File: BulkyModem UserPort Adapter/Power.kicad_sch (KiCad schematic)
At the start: 14 parts, among them Q1 2N3904, Q2 2N3904

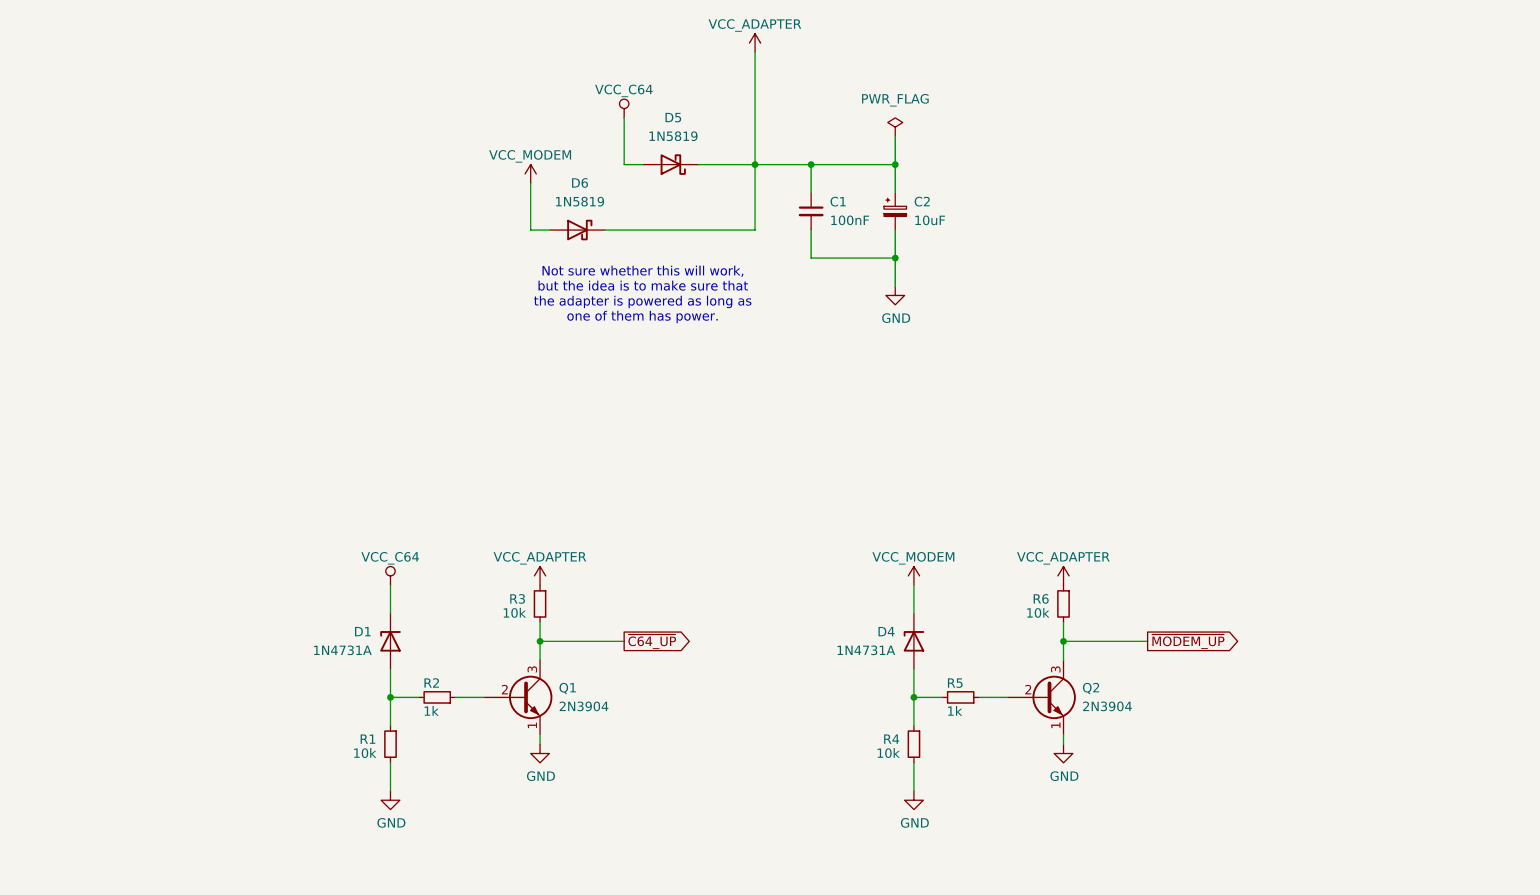
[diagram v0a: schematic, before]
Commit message: Change UserPort transmitter to only enable on both parties present
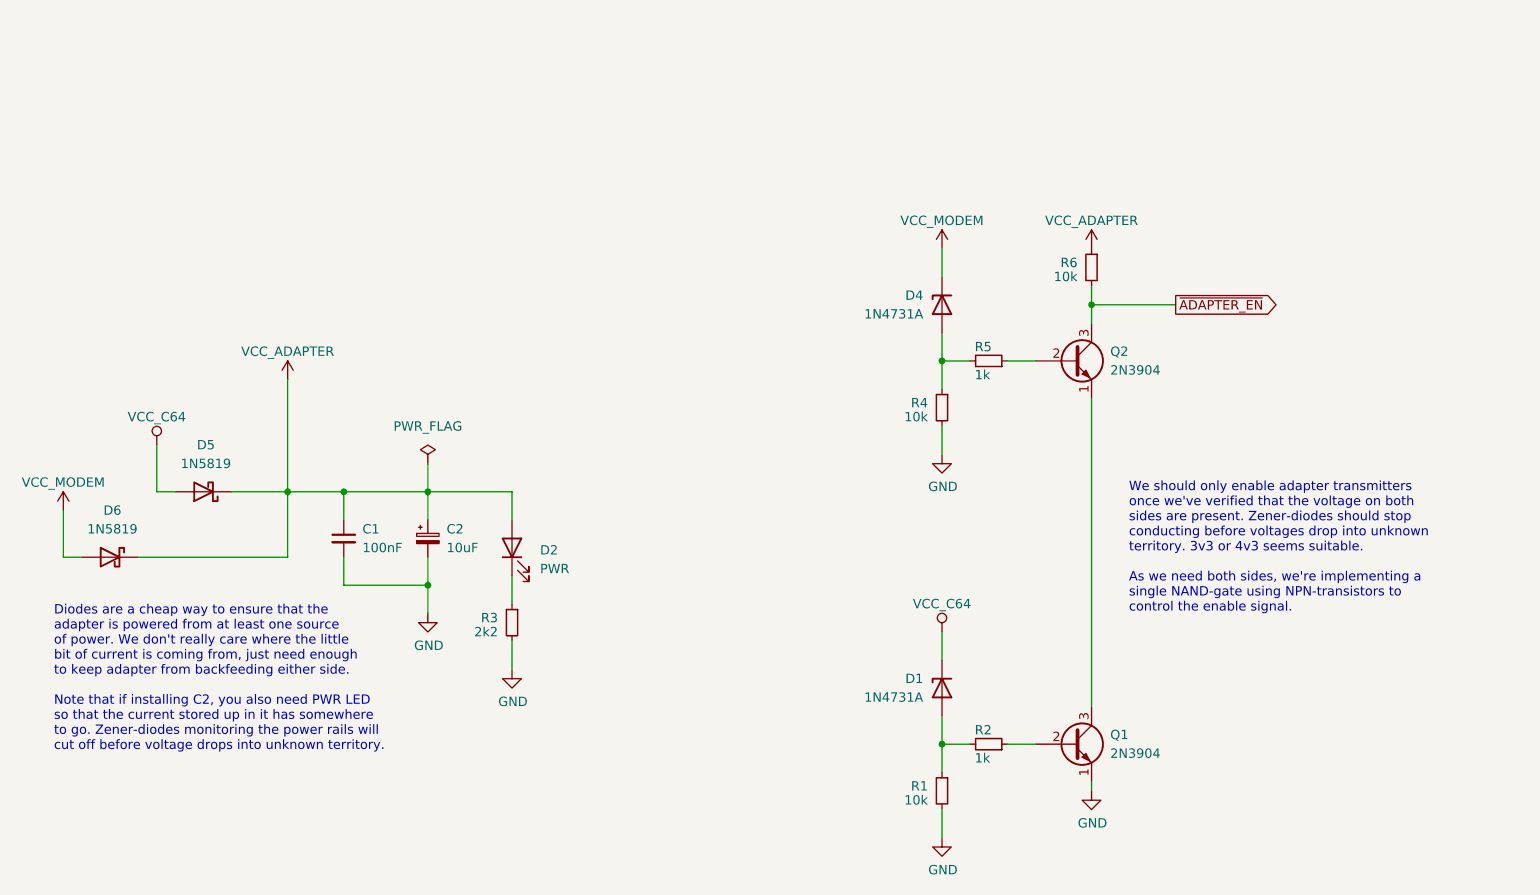
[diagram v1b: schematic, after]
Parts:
- added D2: PWR, LED_THT:LED_D3.0mm, symbol Device:LED
- R3: value 10k -> 2k2
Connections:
- net GND: now also R3.2; no longer Q2.1 (E)
- net VCC_ADAPTER: now also D2.2 (A); no longer R3.1
- net ~{C64_UP}: no longer names the net of Q1.3 (C)
- net ~{C64_UP}: now also Q2.1 (E); no longer R3.2
- net ~{MODEM_UP} renamed ~{ADAPTER_EN}
- new net: D2.1 (K), R3.1
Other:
- note added: "Diodes are a cheap way to ensure that the adapter is powered from at least one source of power. We don't really care where the little bit of current is coming from, just need enough to keep adapter from backfeeding either side. Note that if installing C2, you also need PWR LED so that the current stored up in it has somewhere to go. Zener-diodes monitoring the power rails will cut off before volt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"
- note added: "We should only enable adapter transmitters once we've verified that the voltage on both sides are present. Zener-diodes should stop conducting before voltages drop into unknown territory. 3v3 or 4v3 seems suitable. As we need both sides, we're implementing a single NAND-gate using NPN-transistors to control the enable signal."
- note removed: "Not sure whether this will work, but the idea is to make sure that the adapter is powered as long as one of them has power."
- title: (none) -> Power and control
- moved on the sheet: C1, C2, D1, D4, D5, D6, Q1, Q2, R1, R2, R3, R4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

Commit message: Exported files
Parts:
- added D3: EN, LED_THT:LED_D3.0mm, symbol Device:LED
- added R7: 2k2, resistor:R_Axial_DIN0207_L6.3mm_D2.5mm_P10.16mm_Horizontal, symbol Device:R_Small
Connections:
- net VCC_ADAPTER: now also D3.2 (A)
- net ~{ADAPTER_EN}: now also R7.2
- new net: D3.1 (K), R7.1
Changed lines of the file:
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@@
+	)
+	(junction
+		(at 210.82 62.23)
+		(diameter 0)
+		(color 0 0 0 0)
 	)
 	(junction
@@
 	(wire
 		(pts
+			(xy 210.82 50.8) (xy 210.82 54.61)
+		)
+		(stroke
+			(width 0)
+			(type default)
+		)
+	)
+	(wire
+		(pts
 			(xy 97.79 100.33) (xy 109.22 100.33)
 		)
@@
 	(wire
 		(pts
+			(xy 210.82 62.23) (xy 219.71 62.23)
+		)
+		(stroke
+			(width 0)
+			(type default)
+		)
+	)
+	(wire
+		(pts
 			(xy 72.39 87.63) (xy 74.93 87.63)
 		)
@@
 		(pts
 			(xy 90.17 72.39) (xy 90.17 87.63)
+		)
+		(stroke
+			(width 0)
+			(type default)
+		)
+	)
+	(wire
+		(pts
+			(xy 210.82 59.69) (xy 210.82 62.23)
 		)
 		(stroke
@@
 	(global_label "~{ADAPTER_EN}"
 		(shape output)
-		(at 210.82 62.23 0)
+		(at 219.71 62.23 0)
 		(fields_autoplaced yes)
 		(effects
@@
 		)
 		(property "Intersheetrefs" "${INTERSHEET_REFS}"
-			(at 224.7019 62.23 0)
+			(at 233.5919 62.23 0)
 			(effects
 				(font
@@
 	)
 	(symbol
+		(lib_id "Device:LED")
+		(at 210.82 46.99 90)
+		(unit 1)
+		(exclude_from_sim no)
+		(in_bom yes)
+		(on_board yes)
+		(dnp no)
+		(fields_autoplaced yes)
+		(property "Reference" "D3"
+			(at 214.63 47.3074 90)
+			(effects
+				(font
+					(size 1.27 1.27)
+				)
+				(justify right)
+			)
+		)
+		(property "Value" "EN"
+			(at 214.63 49.8474 90)
+			(effects
+				(font
+					(size 1.27 1.27)
+				)
+				(justify right)
+			)
+		)
+		(property "Footprint" "LED_THT:LED_D3.0mm"
+			(at 210.82 46.99 0)
+			(effects
+				(font
+					(size 1.27 1.27)
+				)
+				(hide yes)
+			)
+		)
+		(property "Datasheet" "~"
+			(at 210.82 46.99 0)
+			(effects
+				(font
+					(size 1.27 1.27)
+				)
+				(hide yes)
+			)
+		)
+		(property "Description" "Light emitting diode"
+			(at 210.82 46.99 0)
+			(effects
+				(font
+					(size 1.27 1.27)
+				)
+				(hide yes)
+			)
+		)
+		(pin "1"
+		)
+		(pin "2"
+		)
+		(instances
+			(project "BulkyModem UserPort Adapter"
+				(path "/64998014-ce0c-479a-b7fa-62fb0232fe84/84bc67ce-40dd-4f01-8688-02db081027e5"
+					(reference "D3")
+					(unit 1)
+				)
+			)
+		)
+	)
+	(symbol
 		(lib_id "Device:C_Polarized_Small")
 		(at 109.22 93.98 0)
@@
 	(symbol
 		(lib_id "Device:R_Small")
+		(at 210.82 57.15 0)
+		(unit 1)
+		(exclude_from_sim no)
+		(in_bom yes)
+		(on_board yes)
+		(dnp no)
+		(property "Reference" "R7"
+			(at 212.725 56.515 0)
+			(effects
+				(font
+					(size 1.27 1.27)
+				)
+				(justify left)
+			)
+		)
+		(property "Value" "2k2"
+			(at 212.725 58.42 0)
+			(effects
+				(font
+					(size 1.27 1.27)
+				)
+				(justify left)
+			)
+		)
+		(property "Footprint" "resistor:R_Axial_DIN0207_L6.3mm_D2.5mm_P10.16mm_Horizontal"
+			(at 210.82 57.15 0)
+			(effects
+				(font
+					(size 1.27 1.27)
+				)
+				(hide yes)
+			)
+		)
+		(property "Datasheet" "~"
+			(at 210.82 57.15 0)
+			(effects
+				(font
+					(size 1.27 1.27)
+				)
+				(hide yes)
+			)
+		)
+		(property "Description" "Resistor, small symbol"
+			(at 210.82 57.15 0)
+			(effects
+				(font
+					(size 1.27 1.27)
+				)
+				(hide yes)
+			)
+		)
+		(pin "2"
+		)
+		(pin "1"
+		)
+		(instances
+			(project "BulkyModem UserPort Adapter"
+				(path "/64998014-ce0c-479a-b7fa-62fb0232fe84/84bc67ce-40dd-4f01-8688-02db081027e5"
+					(reference "R7")
+					(unit 1)
+				)
+			)
+		)
+	)
+	(symbol
+		(lib_id "Device:R_Small")
 		(at 199.39 57.15 0)
 		(mirror y)
@@
 					(unit 1)
 				)
+			)
+		)
+	)
+	(symbol
+		(lib_id "power:VCC")
+		(at 210.82 43.18 0)
+		(unit 1)
+		(exclude_from_sim no)
+		(in_bom yes)
+		(on_board yes)
+		(dnp no)
+		(property "Reference" "#PWR015"
+			(at 210.82 46.99 0)
+			(effects
+				(font
+					(size 1.27 1.27)
+				)
+				(hide yes)
+			)
+		)
+		(property "Value" "VCC_ADAPTER"
+			(at 210.82 39.37 0)
+			(effects
+				(font
+					(size 1.27 1.27)
+				)
+			)
+		)
+		(property "Footprint" ""
+			(at 210.82 43.18 0)
+			(effects
+				(font
+					(size 1.27 1.27)
+				)
+				(hide yes)
+			)
+		)
+		(property "Datasheet" ""
+			(at 210.82 43.18 0)
+			(effects
+				(font
+					(size 1.27 1.27)
+				)
+				(hide yes)
+			)
+		)
+		(property "Description" "Power symbol creates a global label with name \"VCC\""
+			(at 210.82 43.18 0)
+			(effects
+				(font
+					(size 1.27 1.27)
+				)
+				(hide yes)
+			)
+		)
+		(pin "1"
+		)
+		(instances
+			(project "BulkyModem UserPort Adapter"
+				(path "/64998014-ce0c-479a-b7fa-62fb0232fe84/84bc67ce-40dd-4f01-8688-02db081027e5"
+					(reference "#PWR015")
+					(unit 1)
+				)
